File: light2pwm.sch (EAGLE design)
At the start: 8 parts, among them IC2 QUAD_OPAMPP

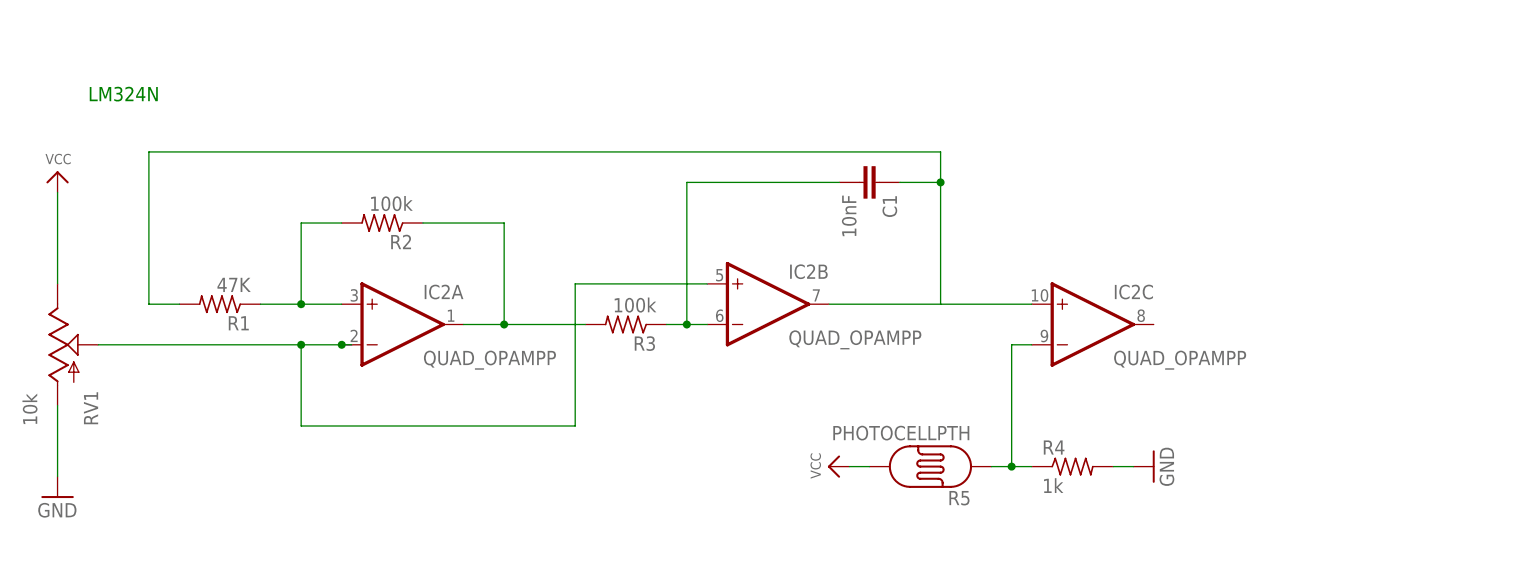
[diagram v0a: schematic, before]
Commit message: pwm output pin added, next add transistor
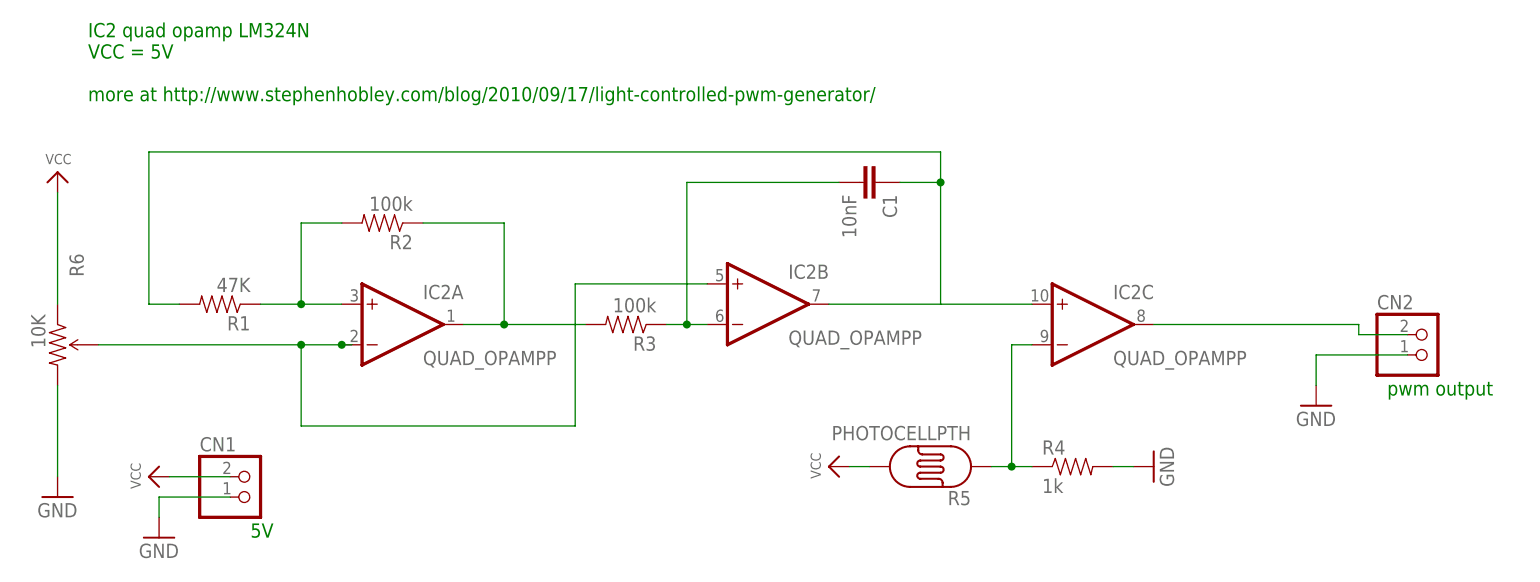
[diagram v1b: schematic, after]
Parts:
- removed RV1: 10k, SparkFun-Electromechanical:POT100K_3362U
- added CN1, CN2: (no value), adafruit:JST_2PIN-THM
- added R6: 10K, SparkFun-Electromechanical:TRIMPOT-PTH-KNOB
- R1, R2, R3, R4: device adafruit:R-US_0414/15 -> SparkFun-Resistors:RESISTOREZ
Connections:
- new net N$7: CN2.1, IC2C.OUT
- net GND: now also CN1.2, CN2.2, R6.CW; no longer RV1.A
- net N$4: now also R6.WIPER; no longer RV1.S
- net VCC: now also CN1.1, R6.CCW; no longer RV1.E
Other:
- note added: "5V"
- note added: "IC2 quad opamp LM324N VCC = 5V more at http://www.stephenhobley.com/blog/2010/09/17/light-controlled-pwm-generator/"
- note added: "pwm output"
- note removed: "LM324N"
